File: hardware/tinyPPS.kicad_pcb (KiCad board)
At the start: 2 copper layers, 60 x 37 mm, 64 parts, among them IC1 AP2205-33Y-13, IC2 AP33772SDKZ-13-FA01, J1 USB_C_Receptacle_USB2.0_14P, J2 187-3802, J3 187-3802, J5 SM03B-SRSS-TB_LF__SN_, Q1 DMN3009SFG-7, Q2 DMN3009SFG-7, Q3 BSS123, Q4 BSS123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

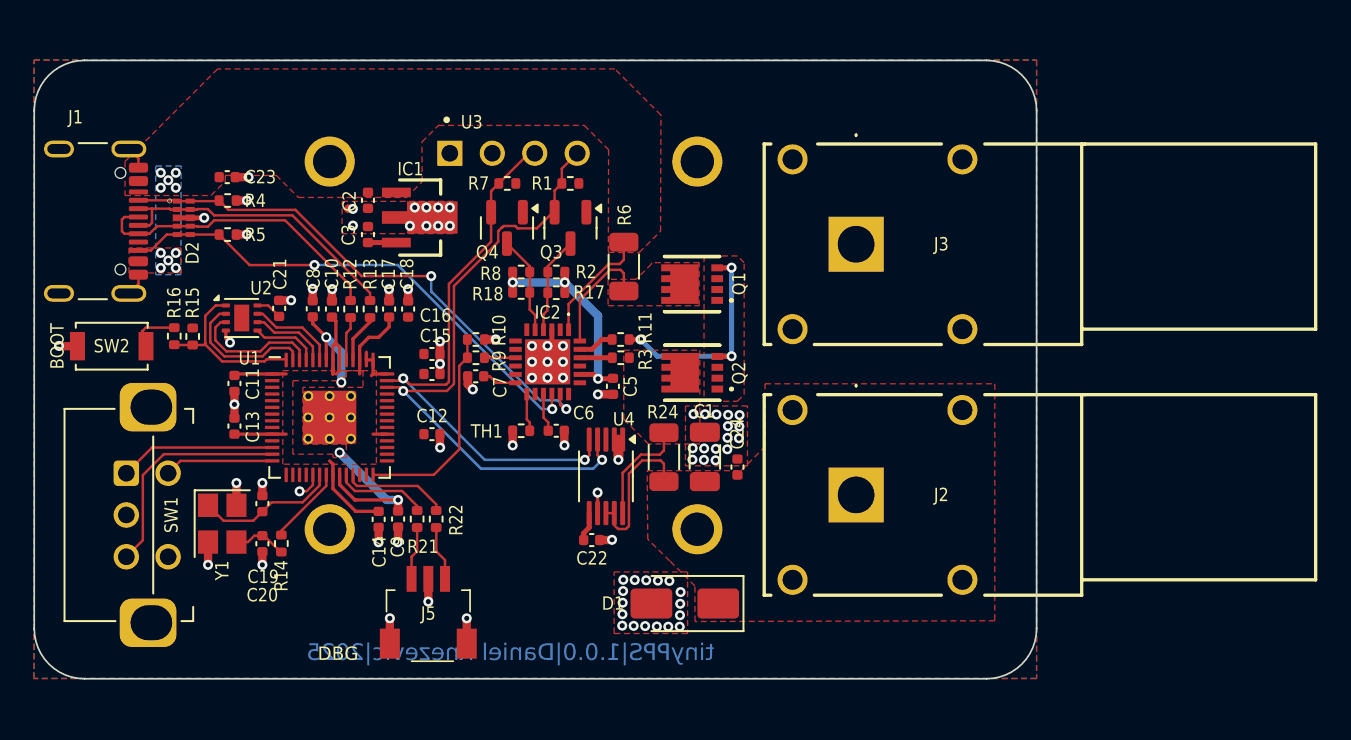
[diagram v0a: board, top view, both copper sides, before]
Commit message: Update schematic with output capacitors
- Add x5 10uF and x1 100uF capacitors to the output
- Move INA226 to be after output capacitors to measure the load and not current of charging capacitors
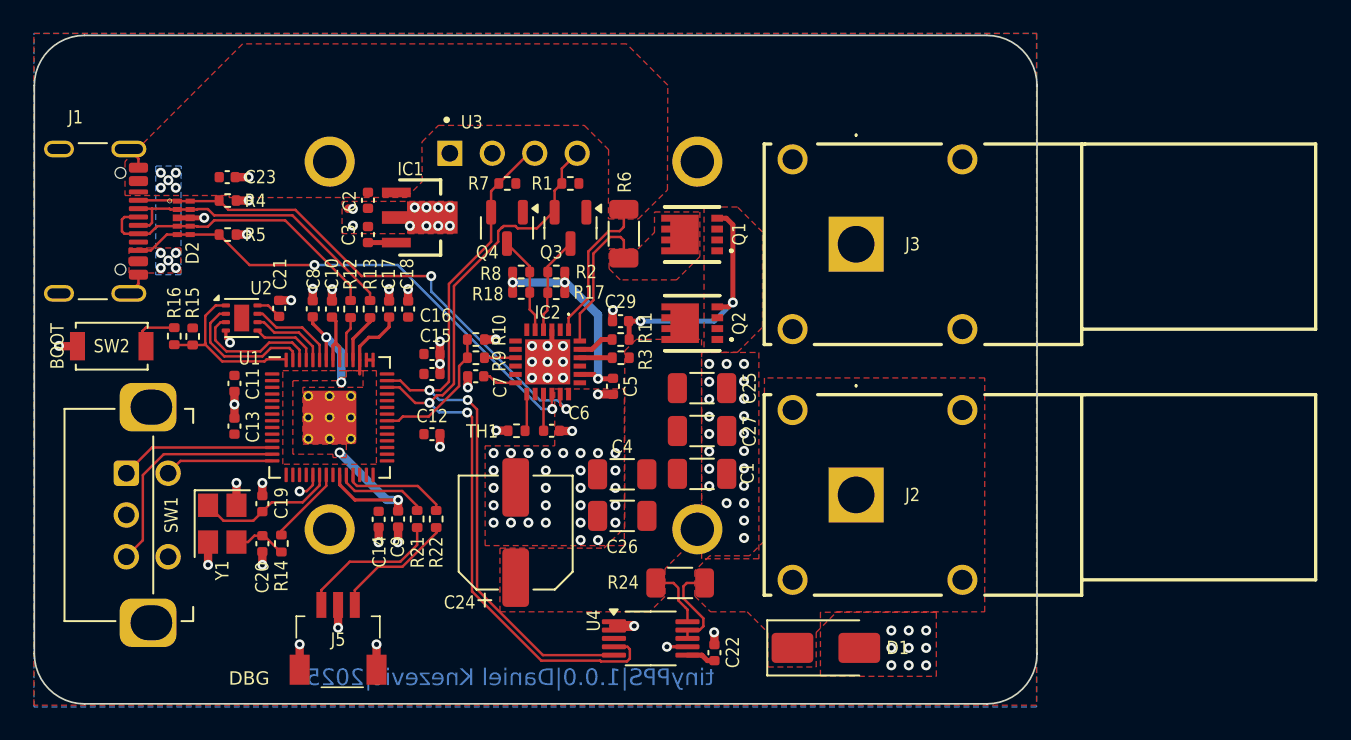
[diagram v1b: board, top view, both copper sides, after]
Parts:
- added C25: 10u, Capacitor_SMD:C_1206_3216Metric, F.Cu at (123.1, 92.9)
- added C26: 10u, Capacitor_SMD:C_1206_3216Metric, F.Cu at (118.3, 100.6)
- added C27: 10u, Capacitor_SMD:C_1206_3216Metric, F.Cu at (123.1, 95.5)
- added C29: 100n, Capacitor_SMD:C_0402_1005Metric, F.Cu at (118.2, 88.9)
- added C4: 10u, Capacitor_SMD:C_1206_3216Metric, F.Cu at (118.3, 98.1)
- C24: value 100n -> 100u; footprint Capacitor_SMD:C_0402_1005Metric -> Capacitor_SMD:CP_Elec_6.3x7.7
- moved C24 13.8 mm to (111.9, 101.6)
- moved U4 10.1 mm to (120.0, 107.9), turned to 0 degrees
- moved C22 9.96 mm to (123.8, 108.7), turned to 90 degrees
- moved D1 8.85 mm to (130.5, 108.5), turned to 0 degrees
- moved R24 7.59 mm to (121.8, 104.6), turned to 0 degrees
- moved J5 5.62 mm to (101.3, 108.3)
- moved Q1 2.97 mm to (121.2, 83.7)
- moved Q2 2.97 mm to (121.2, 89.0)
- moved R6 1.97 mm to (118.4, 83.7)
- moved C1 1.03 mm to (123.1, 98.0), turned to 0 degrees
- moved C6 0.28 mm to (114.1, 95.5)
- moved TH1 0.28 mm to (112.0, 95.5)
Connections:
- C1 pad 1: /VBUS_PD -> /VIN+
- C24 pad 1: /VBUS_PD -> /VIN+
- U1 pad 28: /PD_INT -> unconnected-(U1-GPIO17-Pad28)
- U1 pad 35: unconnected-(U1-GPIO23-Pad35) -> /PD_INT
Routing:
- net +3V3: track 25.8 -> 9.47 mm
- net /SDA: track 37.8 -> 49.2 mm
- net /SCL: track 34.2 -> 44.1 mm
- net Net-(J5-Pad1): track 3.21 -> 8.78 mm
- net /PD_INT: track 12.4 -> 7.96 mm
- net Net-(J5-Pad3): track 3.29 -> 7.50 mm
- net /VBUS_PD: track 8.42 -> 5.23 mm
- net /VIN+: track 6.06 -> 3.21 mm
- net VBUS: track 6.45 -> 8.42 mm
- net Net-(IC2-VCC): track 6.43 -> 8.40 mm
- net Net-(Q1-G): track 13.6 -> 14.6 mm, vias 3 -> 2
- net GND: track 38.5 -> 38.4 mm, vias 85 -> 111
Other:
- board size 60 x 37 mm -> 60 x 40 mm
